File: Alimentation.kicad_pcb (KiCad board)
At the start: 2 copper layers, 50 x 50 mm, 25 parts, among them P1 Prise_Equilibrage, P10 CONN_01X02, P2 Prise_Alim, P3 Prise_Batterie, P4 ConnecteurBippeur, P5 CONN_01X04, P6 CAN_conn, P7 CAN_conn, P8 CONN_01X02, P9 CONN_01X02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

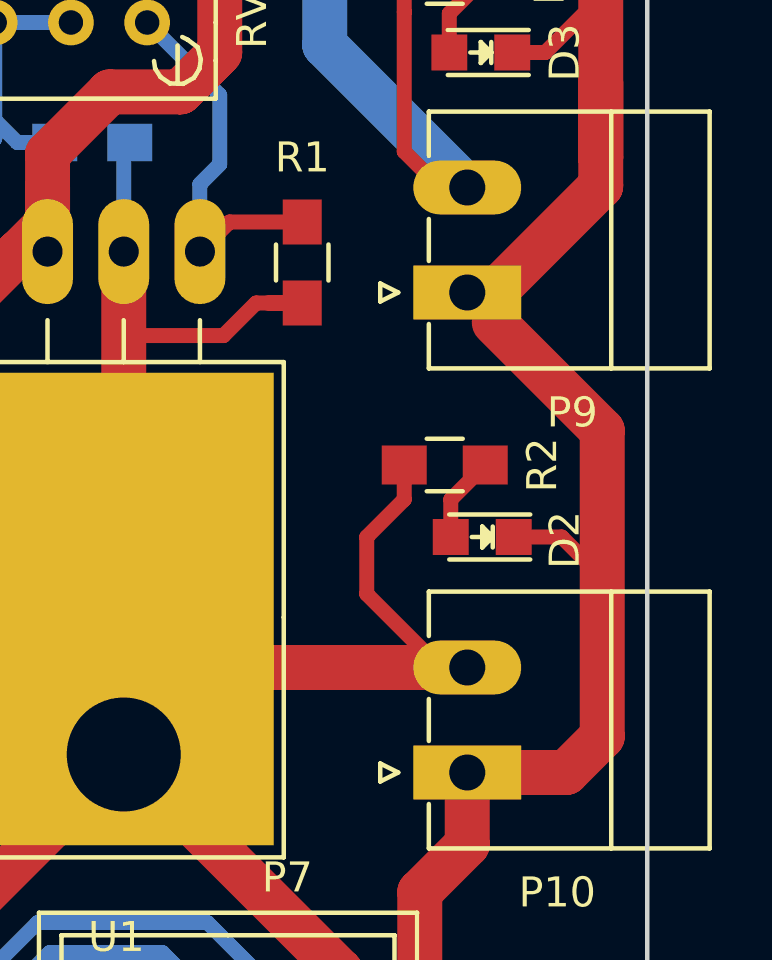
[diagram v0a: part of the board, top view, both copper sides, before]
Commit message: duplique les led sur l'autre face
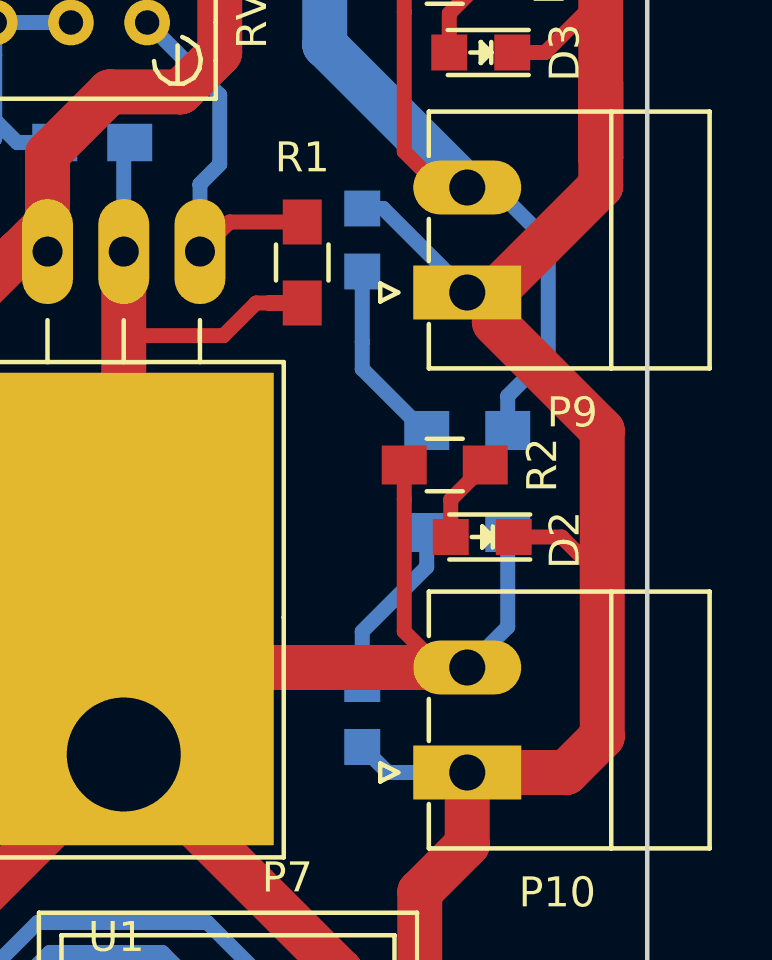
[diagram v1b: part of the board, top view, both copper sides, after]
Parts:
- added D2: LED, LEDs:LED_0805, B.Cu at (140.5, 85.1)
- added D3: LED, LEDs:LED_0805, B.Cu at (140.5, 69.2)
- added R2: R, Resistors_SMD:R_0805_HandSoldering, B.Cu at (144.0, 79.0)
- added R3: R, Resistors_SMD:R_0805_HandSoldering, B.Cu at (144.0, 75.6)
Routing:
- net Non_régulé: track 21.9 -> 32.2 mm
- net GND: track 176.2 -> 184.8 mm
- net Net-(D3-Pad2): track 3.00 -> 9.25 mm
- net Net-(D2-Pad2): track 2.88 -> 9.03 mm
- net +9V: track 77.0 -> 81.0 mm
